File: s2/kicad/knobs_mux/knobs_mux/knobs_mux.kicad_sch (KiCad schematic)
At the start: 5 parts, among them J1 Conn_02x06_Odd_Even, J2 Conn_02x08_Odd_Even, J3 Conn_02x05_Odd_Even, U1 74HC4067PW

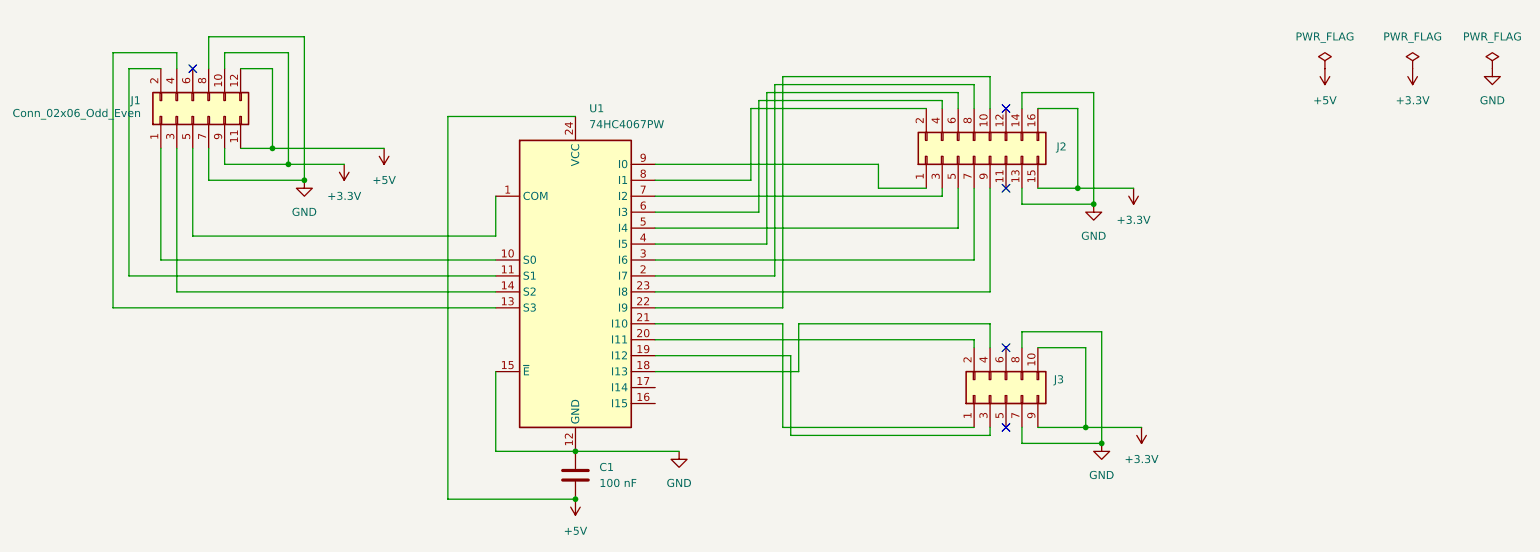
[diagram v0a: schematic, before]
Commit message: added pcbs
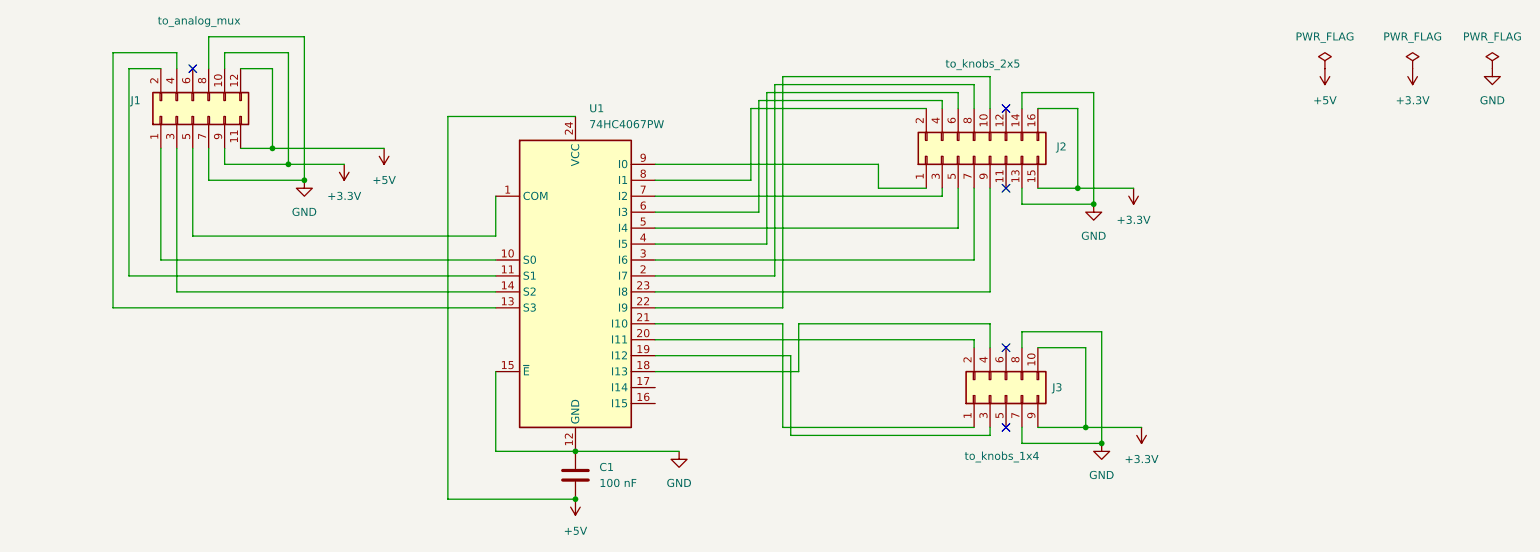
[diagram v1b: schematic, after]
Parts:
- J1: value Conn_02x06_Odd_Even -> to_analog_mux
- J2: value Conn_02x08_Odd_Even -> to_knobs_2x5
- J3: value Conn_02x05_Odd_Even -> to_knobs_1x4
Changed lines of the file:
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@@
 		(on_board yes)
 		(dnp no)
-		(fields_autoplaced yes)
 		(property "Reference" "J3"
-			(at 186.69 97.7899 90)
+			(at 186.436 99.06 90)
 			(effects
 				(font
@@
 			)
 		)
-		(property "Value" "Conn_02x05_Odd_Even"
-			(at 186.69 100.3299 90)
+		(property "Value" "to_knobs_1x4"
+			(at 172.466 109.982 90)
 			(effects
 				(font
@@
 				)
 				(justify right)
-				(hide yes)
 			)
 		)
@@
 			)
 		)
-		(property "Value" "Conn_02x08_Odd_Even"
-			(at 215.392 62.23 90)
+		(property "Value" "to_knobs_2x5"
+			(at 181.356 47.498 90)
 			(effects
 				(font
@@
 				)
 				(justify left)
-				(hide yes)
 			)
 		)
@@
 			)
 		)
-		(property "Value" "Conn_02x06_Odd_Even"
-			(at 20.828 55.372 90)
-			(effects
-				(font
+		(property "Value" "to_analog_mux"
+			(at 43.942 40.64 90)
+			(effects
+				(font
